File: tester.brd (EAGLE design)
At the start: 56 x 67 mm, 72 parts, among them IC1 ATmega8/88/168, K1 NA 05W K, M1 SP6000C-180, P1 250, P2 10k lin, Q1 BC847CSMD, Q2 BC847CSMD, Q3 BC807-40SMD, Q4 8,000 MHz, Q5 BC847CSMD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

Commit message: should know better how to use npn q5
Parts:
- moved D1 0.90 mm to (52.7, 15.9)
- moved Q5 0.66 mm to (40.0, 18.4), turned to 0 degrees
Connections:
- removed net N$23: D1.C, K1.1, Q5.2
- new net N$18: D1.A, K1.12, Q5.3
- net +5V: now also D1.C, K1.1; no longer Q5.3
- net GND: now also Q5.2; no longer D1.A, K1.12
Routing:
- net N$18: track 0.00 -> 16.4 mm
- net N$23: track 12.5 -> 0.00 mm
- net +5V: track 142.0 -> 154.2 mm
- net N$22: track 10.2 -> 7.81 mm
- net V+: track 143.8 -> 144.3 mm

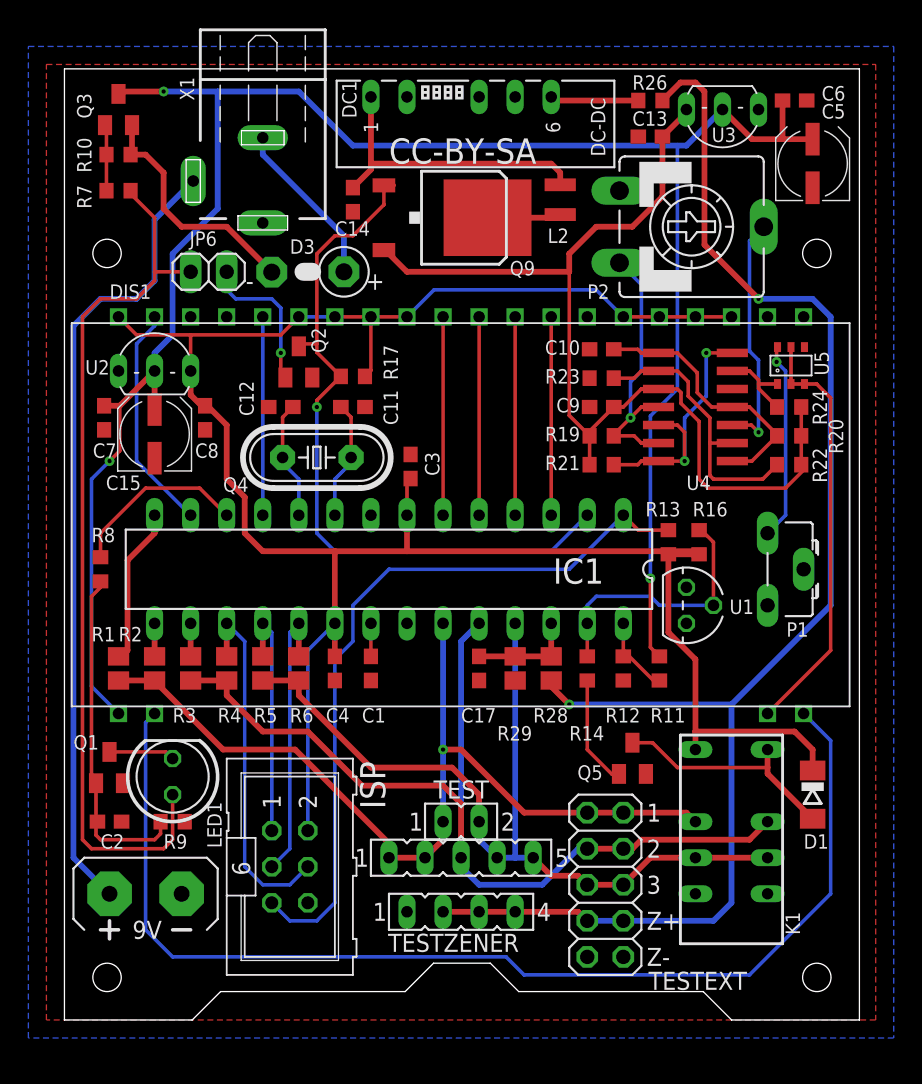
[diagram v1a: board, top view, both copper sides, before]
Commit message: changed all r/c to 0805, resized some pads, hopefully made easier to solder
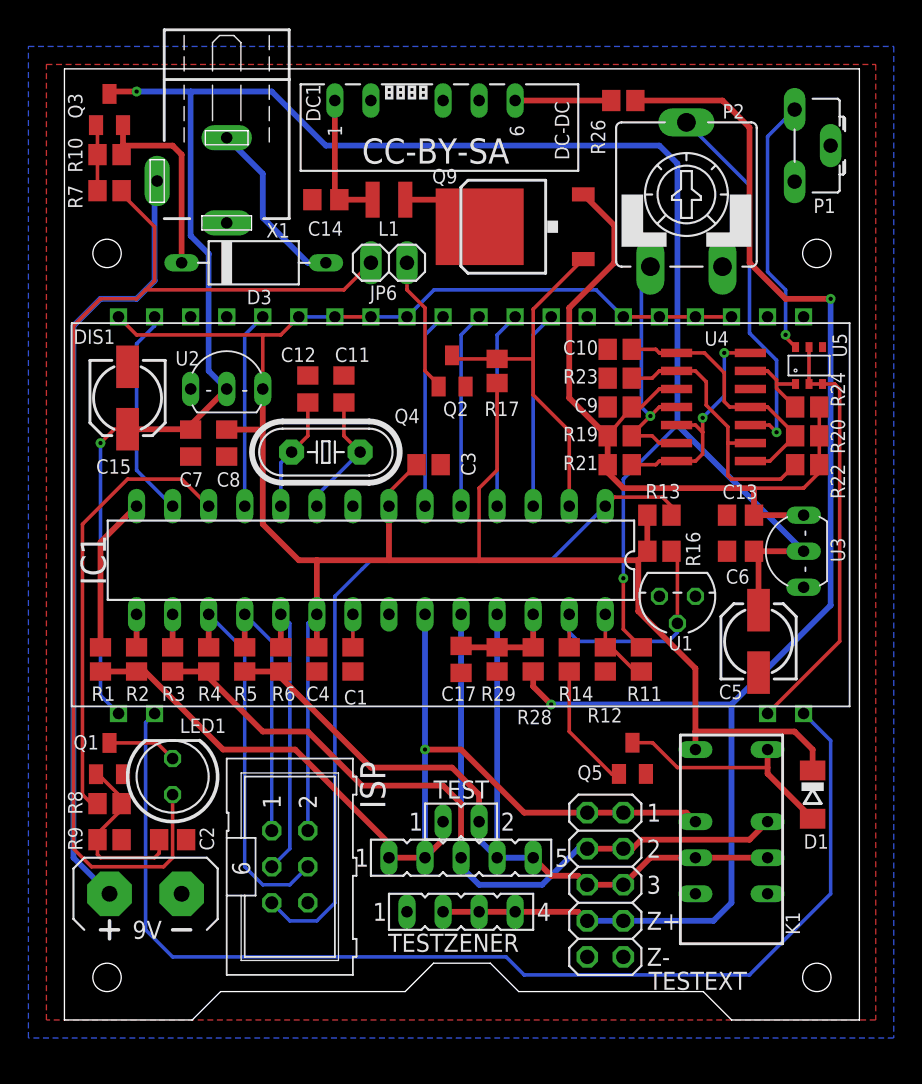
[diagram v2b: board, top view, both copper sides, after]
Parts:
- removed L2: L-1008F 33µ, EagleLibrary_Wuerth_Elektronik_eiSos_Version_6:WE-RFI_1008
- added L1: 33u, inductor-neosid:SM-NE29
- C1, C10, C3, C4, C9: device resistor:C0603 -> resistor:C0805
- C11, C12, C13, C14, C17, C2, C6, C7, C8: device rcl:C0603 -> rcl:C0805
- C15, C5: device rcl:UD-5X5,8_NICHICON -> rcl:153CLV-0505
- D3: device markus:DIODE-3-5A-V -> markus:DIODE-3-10
- R10, R11, R12, R13, R14, R16, R17, R19, R20, R21, R22, R23, R24, R26, R7, R8, R9: device resistor:R0603 -> resistor:R0805
- moved C5 33.9 mm to (48.9, 26.7)
- moved C6 32.0 mm to (47.6, 33.0), turned to 180 degrees
- moved U3 30.7 mm to (52.1, 34.3), turned to 90 degrees
- moved P1 29.9 mm to (51.4, 61.6)
- moved C13 27.4 mm to (47.6, 35.6)
- moved R8 16.5 mm to (3.17, 15.2), turned to 0 degrees
- moved JP6 12.7 mm to (22.9, 53.3)
- moved Q2 10.8 mm to (27.3, 45.7)
- moved R17 10.2 mm to (30.5, 45.7), turned to 270 degrees
- moved C7 6.35 mm to (8.89, 40.6)
- moved U2 5.24 mm to (12.7, 44.5)
- moved C2 4.62 mm to (7.62, 12.7)
- moved R9 4.62 mm to (3.17, 12.7)
- moved Q9 4.49 mm to (31.8, 55.9), turned to 90 degrees
- moved D3 3.86 mm to (13.3, 53.3), turned to 0 degrees
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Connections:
- net GND: now also P2.E; no longer P2.A
- net N$15: now also P2.A; no longer P2.E
- net N$24: now also L1.1; no longer L2.1
- net N$25: now also L1.2; no longer L2.2
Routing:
- net PD0: track 51.3 -> 25.7 mm, vias 1 -> 0
- net PD6: track 12.7 -> 31.4 mm
- net N$21: track 62.6 -> 80.1 mm
- net +5V/2: track 71.8 -> 55.7 mm
- net N$25: track 21.4 -> 9.46 mm
- net N$35: track 24.1 -> 13.1 mm
- net N$16: track 17.2 -> 26.5 mm
- net V+: track 144.3 -> 152.6 mm
- net +5V: track 154.2 -> 160.5 mm
- net PC0: track 64.3 -> 70.3 mm
- net N$1: track 14.0 -> 18.5 mm
- net +30V: track 104.5 -> 107.2 mm
- net N$5: track 17.0 -> 14.3 mm
- net N$7: track 19.3 -> 16.9 mm
- net PC6: track 52.3 -> 54.6 mm
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
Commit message: some change
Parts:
- removed PLATINENSAMMLER: LP_NUMBER08_SILK_TOP, Platinensammler:LP_NUMBER_SILK_TOP
- M1: value SP6000C-180 -> SP6000H-180; device strapubox:SP-6000-C-180 -> strapubox:SP6000H-180
- moved JP6 5.85 mm to (18.4, 57.1), turned to 270 degrees
- moved C14 4.49 mm to (22.9, 57.1), turned to 0 degrees
- moved L1 3.81 mm to (22.9, 54.0)
- moved DC1 3.70 mm to (27.3, 61.6), turned to 270 degrees
- moved Q5 1.42 mm to (39.4, 19.7)
- moved JP4 1.42 mm to (39.4, 10.2)
- moved Q9 0.90 mm to (31.1, 55.2)
- moved D3 0.64 mm to (13.3, 52.7)
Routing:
- net N$21: track 80.1 -> 63.2 mm, vias 0 -> 1
- net N$28: track 6.77 -> 18.9 mm
- net N$3: track 9.64 -> 18.6 mm
- net N$25: track 9.46 -> 17.7 mm
- net +5V/2: track 55.7 -> 61.0 mm
- net N$2: track 80.9 -> 76.7 mm
- net V+: track 152.6 -> 149.0 mm
- net N$7: track 16.9 -> 20.6 mm
- net N$22: track 8.97 -> 7.14 mm
- net N$18: track 16.4 -> 17.6 mm
- net +30V: track 107.2 -> 106.3 mm
- net N$24: track 6.03 -> 5.13 mm
- net N$4: track 19.9 -> 20.6 mm
- net N$5: track 14.3 -> 15.0 mm
- net N$11: track 12.4 -> 13.1 mm
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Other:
- outline, holes or cut-outs redrawn

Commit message: switch case back, oshpark dru
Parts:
- M1: value SP6000H-180 -> SP6000C-180; device strapubox:SP6000H-180 -> strapubox:SP-6000-C-180
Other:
- outline, holes or cut-outs redrawn
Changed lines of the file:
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@@
 </class>
 </classes>
-<designrules name="bilex *">
-<description language="de">&lt;b&gt;EAGLE Design Rules&lt;/b&gt;
+<designrules name="oshpark">
+<description language="de">&lt;a href=&quot;http://oshpark.com/guidelines&quot;&gt;http://oshpark.com/guidelines&lt;/a&gt;</description>
+<description language="en">&lt;b&gt;Laen's PCB Order Design Rules&lt;/b&gt;
 &lt;p&gt;
-The default Design Rules have been set to cover
-a wide range of applications. Your particular design
-may have different requirements, so please make the
-necessary adjustments and save your customized
-design rules under a new name.</description>
+Please make sure your boards conform to these design rules.</description>
 <param name="layerSetup" value="(1*16)"/>
-<param name="mtCopper" value="0.035mm 0.035mm 0.035mm 0.035mm 0.035mm 0.035mm 0.035mm 0.035mm 0.035mm 0.035mm 0.035mm 0.035mm 0.035mm 0.035mm 0.035mm 0.035mm"/>
-<param name="mtIsolate" value="1.5mm 0.15mm 0.2mm 0.15mm 0.2mm 0.15mm 0.2mm 0.15mm 0.2mm 0.15mm 0.2mm 0.15mm 0.2mm 0.15mm 0.2mm"/>
-<param name="mdWireWire" value="10mil"/>
-<param name="mdWirePad" value="10mil"/>
-<param name="mdWireVia" value="10mil"/>
-<param name="mdPadPad" value="10mil"/>
-<param name="mdPadVia" value="10mil"/>
-<param name="mdViaVia" value="10mil"/>
-<param name="mdSmdPad" value="10mil"/>
-<param name="mdSmdVia" value="10mil"/>
-<param name="mdSmdSmd" value="10mil"/>
+<param name="mtCopper" value="0.0356mm 0.0356mm 0.0356mm 0.0356mm 0.0356mm 0.0356mm 0.0356mm 0.0356mm 0.0356mm 0.0356mm 0.0356mm 0.0356mm 0.0356mm 0.0356mm 0.0356mm 0.0356mm"/>
+<param name="mtIsolate" value="1.5011mm 0.1499mm 0.2007mm 0.1499mm 0.2007mm 0.1499mm 0.2007mm 0.1499mm 0.2007mm 0.1499mm 0.2007mm 0.1499mm 0.2007mm 0.1499mm 0.2007mm"/>
+<param name="mdWireWire" value="6mil"/>
+<param name="mdWirePad" value="6mil"/>
+<param name="mdWireVia" value="6mil"/>
+<param name="mdPadPad" value="6mil"/>
+<param name="mdPadVia" value="6mil"/>
+<param name="mdViaVia" value="6mil"/>
+<param name="mdSmdPad" value="6mil"/>
+<param name="mdSmdVia" value="6mil"/>
+<param name="mdSmdSmd" value="6mil"/>
 <param name="mdViaViaSameLayer" value="8mil"/>
 <param name="mnLayersViaInSmd" value="2"/>
-<param name="mdCopperDimension" value="40mil"/>
-<param name="mdDrill" value="8mil"/>
+<param name="mdCopperDimension" value="15mil"/>
+<param name="mdDrill" value="6mil"/>
 <param name="mdSmdStop" value="0mil"/>
-<param name="msWidth" value="10mil"/>
-<param name="msDrill" value="0.4mm"/>
-<param name="msMicroVia" value="9.99mm"/>
+<param name="msWidth" value="6mil"/>
+<param name="msDrill" value="13mil"/>
+<param name="msMicroVia" value="13mil"/>
 <param name="msBlindViaRatio" value="0.5"/>
 <param name="rvPadTop" value="0.25"/>
@@
 <param name="rvMicroViaOuter" value="0.25"/>
 <param name="rvMicroViaInner" value="0.25"/>
-<param name="rlMinPadTop" value="10mil"/>
+<param name="rlMinPadTop" value="7mil"/>
 <param name="rlMaxPadTop" value="20mil"/>
-<param name="rlMinPadInner" value="10mil"/>
+<param name="rlMinPadInner" value="7mil"/>
 <param name="rlMaxPadInner" value="20mil"/>
-<param name="rlMinPadBottom" value="10mil"/>
+<param name="rlMinPadBottom" value="7mil"/>
 <param name="rlMaxPadBottom" value="20mil"/>
-<param name="rlMinViaOuter" value="8mil"/>
+<param name="rlMinViaOuter" value="7mil"/>
 <param name="rlMaxViaOuter" value="20mil"/>
-<param name="rlMinViaInner" value="8mil"/>
+<param name="rlMinViaInner" value="7mil"/>
 <param name="rlMaxViaInner" value="20mil"/>
 <param name="rlMinMicroViaOuter" value="4mil"/>
@@
 <param name="srMinRoundness" value="0mil"/>
 <param name="srMaxRoundness" value="0mil"/>
-<param name="slThermalIsolate" value="15mil"/>
+<param name="slThermalIsolate" value="10mil"/>
 <param name="slThermalsForVias" value="0"/>
 <param name="dpMaxLengthDifference" value="10mm"/>
@@
 <attribute name="VALUE" x="37.465" y="33.02" size="1.778" layer="27" ratio="10" rot="R180"/>
 </element>
-<element name="M1" library="strapubox" package="SP6000H-180" value="SP6000H-180" x="0" y="0"/>
+<element name="M1" library="strapubox" package="SP-6000-C-180" value="SP6000C-180" x="0" y="0"/>
 <element name="JP6" library="pinhead" package="1X02" value="POWERSW" x="18.415" y="57.15" smashed="yes" rot="R270">
 <attribute name="NAME" x="13.97" y="54.61" size="1.016" layer="25"/>
@@
 </elements>
 <signals>
-<signal name="GND" airwireshidden="yes">
+<signal name="GND">
 <contactref element="U2" pad="GND"/>
 <contactref element="Q1" pad="2"/>
@@
 <contactref element="Q5" pad="2"/>
 <contactref element="P2" pad="E"/>
-<wire x1="51.435" y1="59.055" x2="46.355" y2="53.07" width="0" layer="19" extent="1-1"/>
-<wire x1="48.32" y1="44.45" x2="53.401" y2="47.401" width="0" layer="19" extent="1-1"/>
 </signal>
 <signal name="N$5">

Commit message: silkscreen
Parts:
- moved Q5 0.66 mm to (39.4, 19.0), turned to 270 degrees
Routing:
- net N$18: track 17.6 -> 15.8 mm
- net N$22: track 7.14 -> 6.05 mm
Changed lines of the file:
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@@
 <layer number="27" name="tValues" color="7" fill="1" visible="no" active="yes"/>
 <layer number="28" name="bValues" color="7" fill="1" visible="no" active="yes"/>
-<layer number="29" name="tStop" color="7" fill="3" visible="no" active="yes"/>
-<layer number="30" name="bStop" color="7" fill="6" visible="no" active="yes"/>
+<layer number="29" name="tStop" color="7" fill="3" visible="yes" active="yes"/>
+<layer number="30" name="bStop" color="7" fill="6" visible="yes" active="yes"/>
 <layer number="31" name="tCream" color="7" fill="4" visible="no" active="yes"/>
 <layer number="32" name="bCream" color="7" fill="5" visible="no" active="yes"/>
@@
 <layer number="37" name="tTest" color="7" fill="1" visible="no" active="yes"/>
 <layer number="38" name="bTest" color="7" fill="1" visible="no" active="yes"/>
-<layer number="39" name="tKeepout" color="4" fill="11" visible="yes" active="yes"/>
+<layer number="39" name="tKeepout" color="4" fill="11" visible="no" active="yes"/>
 <layer number="40" name="bKeepout" color="1" fill="11" visible="no" active="yes"/>
-<layer number="41" name="tRestrict" color="4" fill="10" visible="yes" active="yes"/>
+<layer number="41" name="tRestrict" color="4" fill="10" visible="no" active="yes"/>
 <layer number="42" name="bRestrict" color="1" fill="10" visible="no" active="yes"/>
-<layer number="43" name="vRestrict" color="2" fill="10" visible="yes" active="yes"/>
+<layer number="43" name="vRestrict" color="2" fill="10" visible="no" active="yes"/>
 <layer number="44" name="Drills" color="7" fill="1" visible="no" active="yes"/>
 <layer number="45" name="Holes" color="7" fill="1" visible="no" active="yes"/>
@@
 </class>
 </classes>
-<designrules name="oshpark">
+<designrules name="oshpark *">
 <description language="de">&lt;a href=&quot;http://oshpark.com/guidelines&quot;&gt;http://oshpark.com/guidelines&lt;/a&gt;</description>
 <description language="en">&lt;b&gt;Laen's PCB Order Design Rules&lt;/b&gt;
@@
 <param name="mlMinCreamFrame" value="0mil"/>
 <param name="mlMaxCreamFrame" value="0mil"/>
-<param name="mlViaStopLimit" value="0mil"/>
+<param name="mlViaStopLimit" value="0.4mm"/>
 <param name="srRoundness" value="0"/>
 <param name="srMinRoundness" value="0mil"/>
@@
 <attribute name="VALUE" x="45.72" y="15.24" size="1.27" layer="27" rot="R270"/>
 </element>
-<element name="Q5" library="transistor-npn" package="SOT23" value="BC847CSMD" x="39.377" y="19.701" smashed="yes">
-<attribute name="NAME" x="35.497" y="18.196" size="1.016" layer="25"/>
-<attribute name="VALUE" x="37.472" y="16.526" size="1.27" layer="27"/>
+<element name="Q5" library="transistor-npn" package="SOT23" value="BC847CSMD" x="39.386" y="19.043" smashed="yes" rot="R270">
+<attribute name="NAME" x="37.049" y="18.352" size="1.016" layer="25" rot="R90"/>
+<attribute name="VALUE" x="36.211" y="20.948" size="1.27" layer="27" rot="R270"/>
 </element>
 <element name="R14" library="resistor" package="R0805" value="4k7" x="35.56" y="25.4" smashed="yes" rot="R270">
@@
 <contactref element="R14" pad="2"/>
 <contactref element="Q5" pad="1"/>
-<wire x1="35.56" y1="24.55" x2="35.56" y2="21.468" width="0.254" layer="1"/>
-<wire x1="35.56" y1="21.468" x2="38.427" y2="18.601" width="0.254" layer="1"/>
+<wire x1="35.56" y1="24.55" x2="35.56" y2="22.103" width="0.254" layer="1"/>
+<wire x1="35.56" y1="22.103" x2="37.67" y2="19.993" width="0.25" layer="1"/>
+<wire x1="37.67" y1="19.993" x2="38.286" y2="19.993" width="0.25" layer="1"/>
 </signal>
 <signal name="PC3">
@@
 <wire x1="10.16" y1="45.72" x2="10.16" y2="53.975" width="0.4064" layer="16"/>
 <wire x1="8.89" y1="65.405" x2="36.83" y2="65.405" width="0.4064" layer="16"/>
-<via x="39.37" y="31.115" extent="1-16" drill="0.4"/>
+<via x="39.37" y="31.115" extent="1-16" drill="0.4" alwaysstop="yes"/>
 <via x="5.08" y="65.405" extent="1-16" drill="0.4"/>
 <wire x1="5.08" y1="65.405" x2="3.345" y2="65.405" width="0.4064" layer="1"/>
@@
 <wire x1="49.53" y1="17.78" x2="49.53" y2="19.05" width="0.4064" layer="1"/>
 <wire x1="43.18" y1="17.78" x2="49.53" y2="17.78" width="0.254" layer="1"/>
-<wire x1="43.18" y1="17.78" x2="40.64" y2="20.32" width="0.254" layer="1"/>
-<wire x1="40.64" y1="20.32" x2="39.858" y2="20.32" width="0.254" layer="1"/>
-<wire x1="39.858" y1="20.32" x2="39.377" y2="20.801" width="0.254" layer="1"/>
+<wire x1="43.18" y1="17.78" x2="41.749" y2="17.78" width="0.25" layer="1"/>
+<wire x1="41.749" y1="17.78" x2="40.486" y2="19.043" width="0.25" layer="1"/>
 </signal>
 </signals>

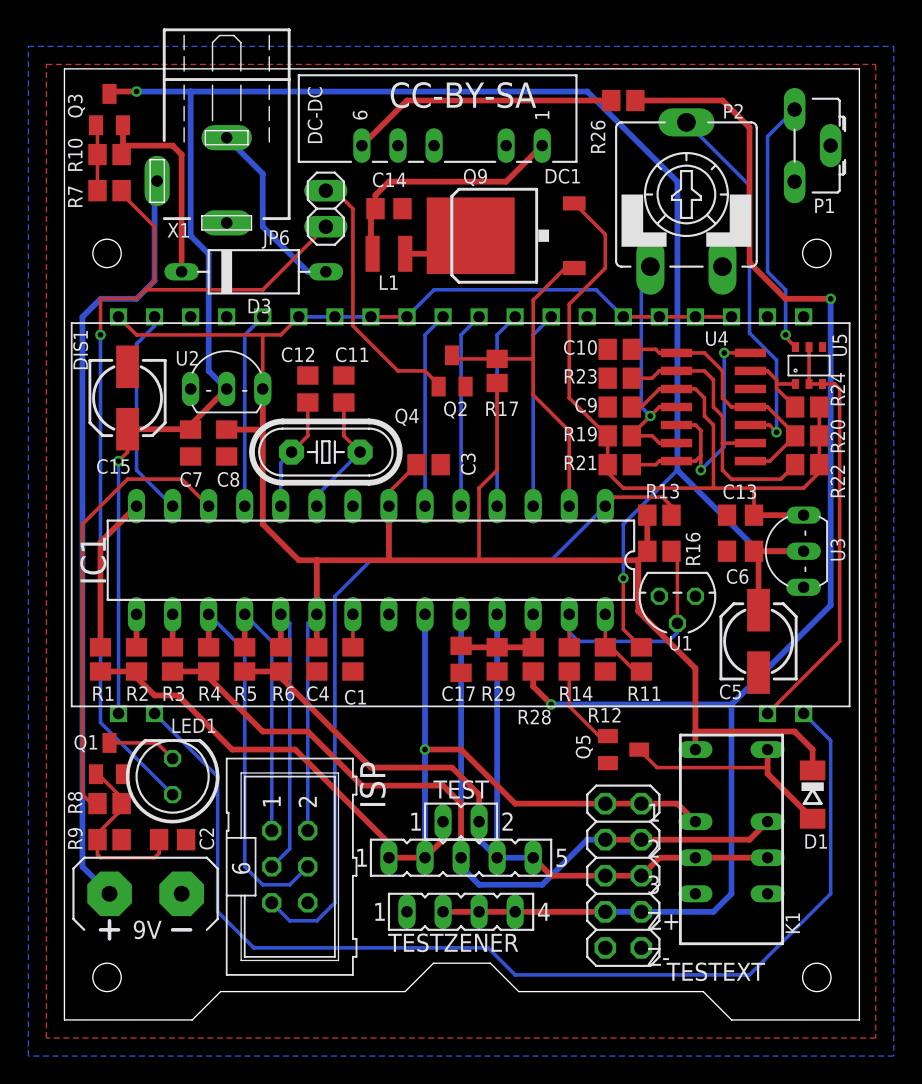
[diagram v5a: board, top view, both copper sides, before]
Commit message: 0805 pad size and silk print
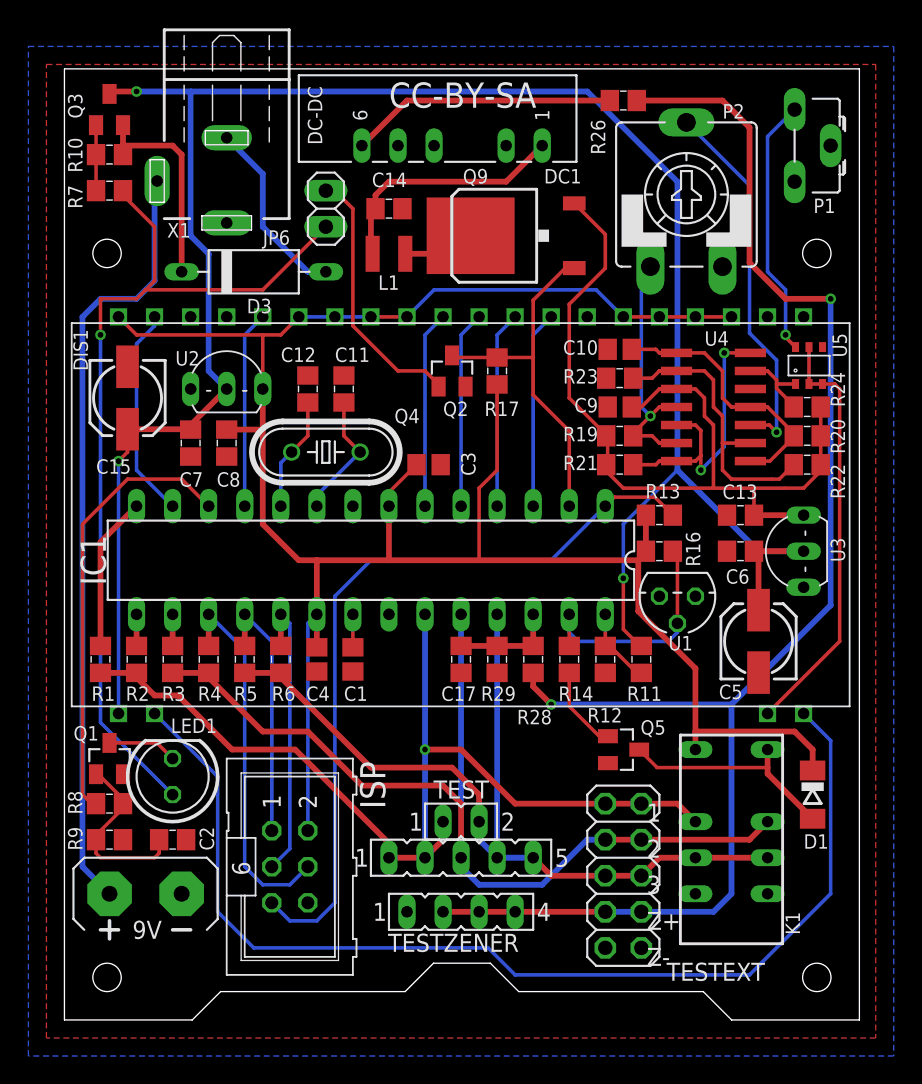
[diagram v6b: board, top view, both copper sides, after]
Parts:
- M1: device strapubox:SP-6000-C-180 -> strapubox:SP6000C-180
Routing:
- net PD0: track 25.2 -> 28.3 mm
- net +5V: track 160.5 -> 159.9 mm
- net PC4: track 18.1 -> 17.5 mm
